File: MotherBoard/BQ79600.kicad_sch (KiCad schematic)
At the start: 10 parts, among them IC501 BQ79600PWRQ1

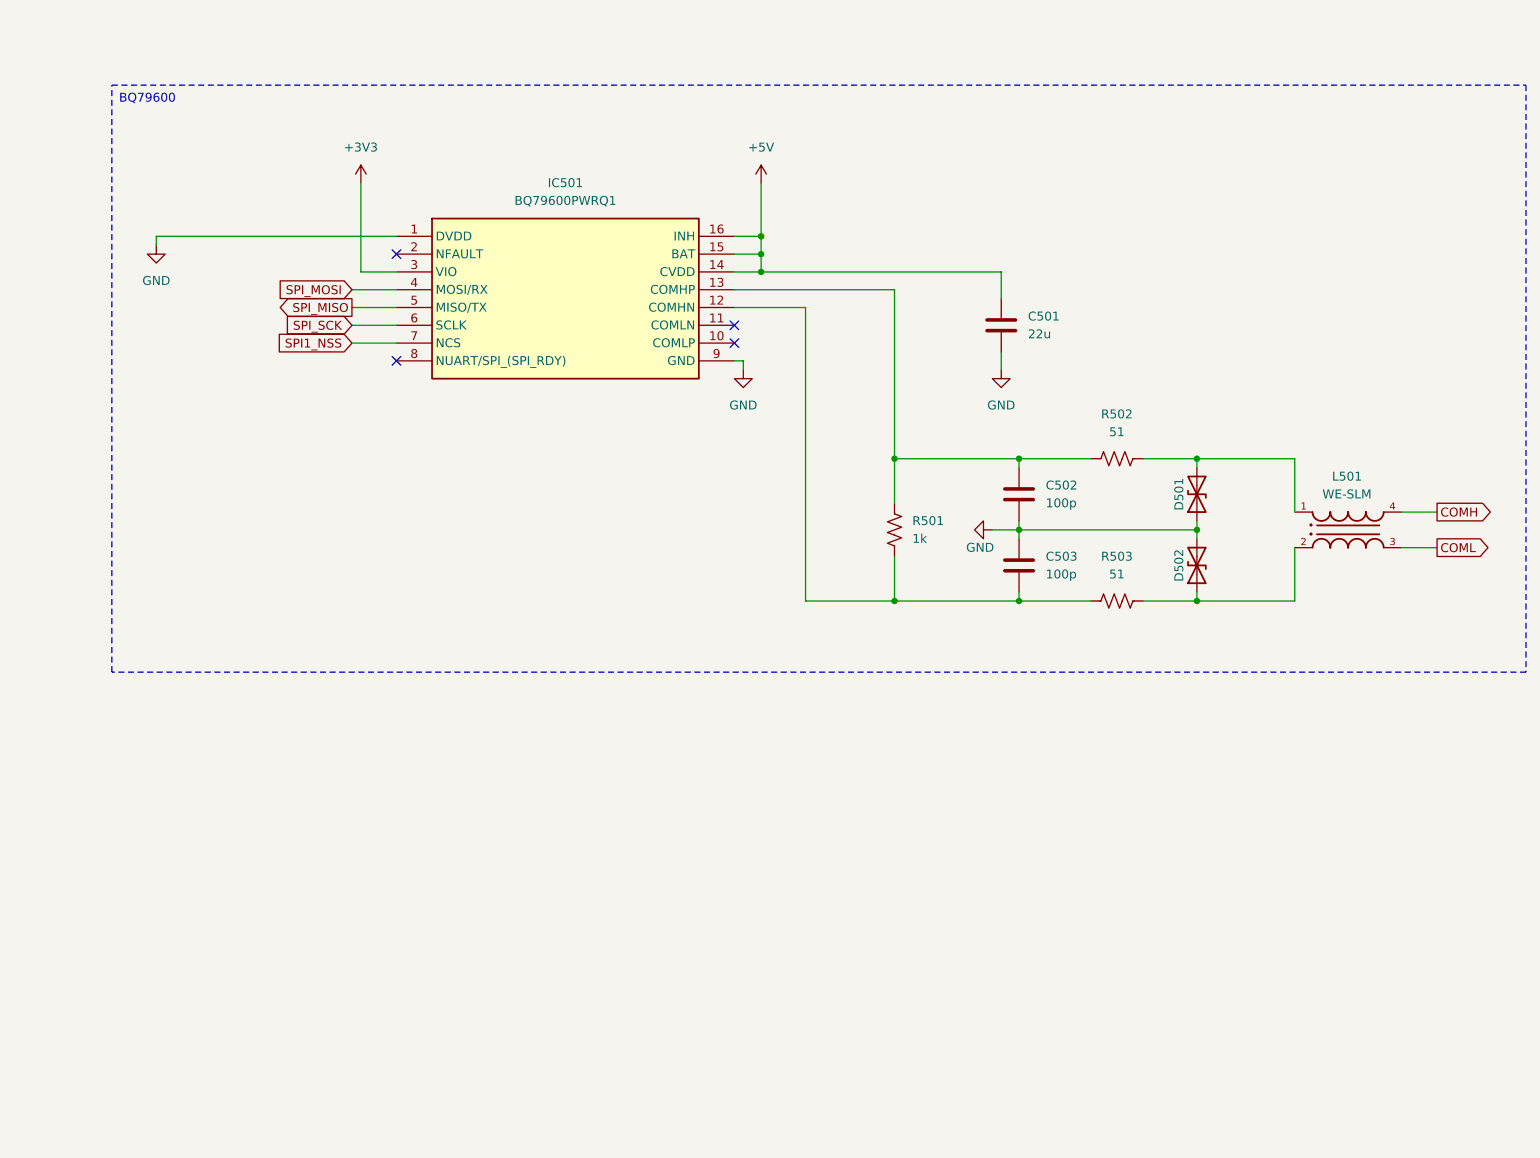
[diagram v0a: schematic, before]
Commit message: Fixed BQ79600 + minor changes
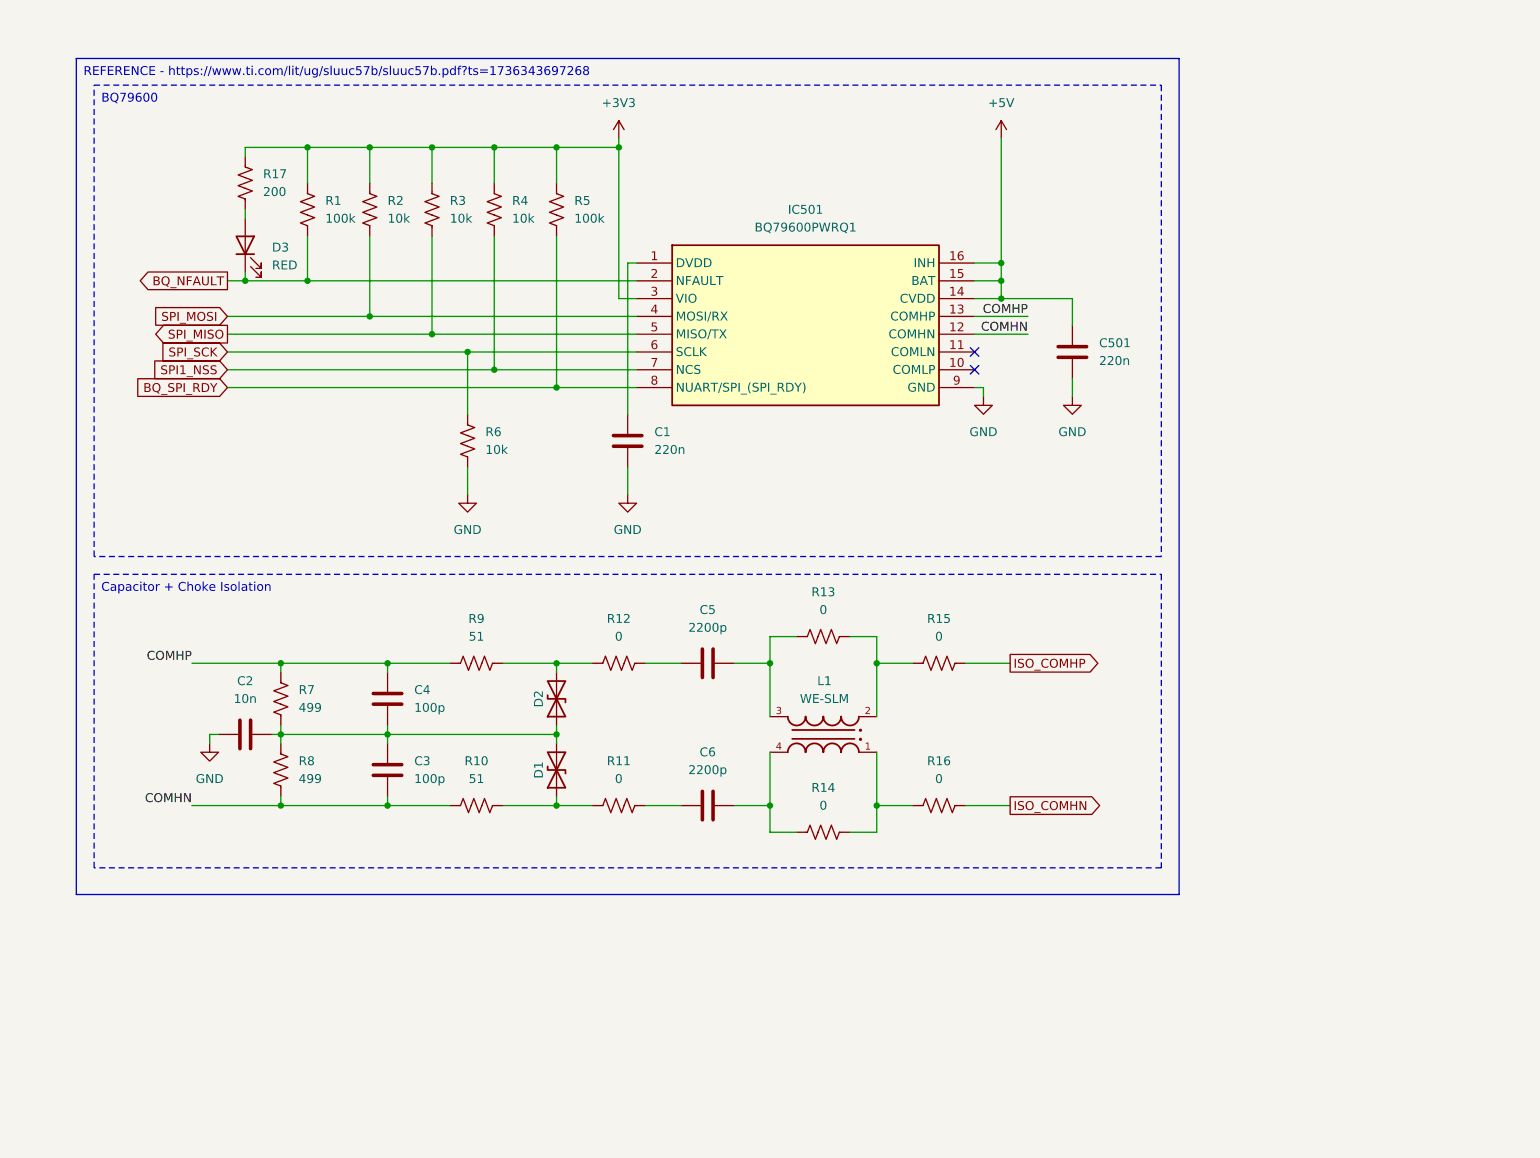
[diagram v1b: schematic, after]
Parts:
- removed C502, C503: 100p, symbol Device:C
- removed D501, D502: D_TVS, Diode_SMD:D_SOD-323, symbol Device:D_TVS
- removed L501: WE-SLM, Transformer_WURTH:Isolation_Transformer, symbol Isolation_Transformer:WE-SLM
- removed R501: 1k, symbol Device:R_US
- removed R502, R503: 51, symbol Device:R_US
- added C1: 220n, symbol Device:C
- added C2: 10n, symbol Device:C
- added C3, C4: 100p, symbol Device:C
- added C5, C6: 2200p, symbol Device:C
- added D1, D2: D_TVS, Diode_SMD:D_SOD-323, symbol Device:D_TVS
- added D3: RED, symbol Device:LED
- added L1: WE-SLM, WE-SLM:WE-SLM, symbol CommonModeChoke_Wurth:WE-SLM
- added R1, R5: 100k, symbol Device:R_US
- added R10, R9: 51, symbol Device:R_US
- added R11, R12, R13, R14, R15, R16: 0, symbol Device:R_US
- added R17: 200, symbol Device:R_US
- added R2, R3, R4, R6: 10k, symbol Device:R_US
- added R7, R8: 499, symbol Device:R_US
- C501: value 22u -> 220n
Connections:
- net +3V3: now also R1.1, R17.1, R2.1, R3.1, R4.1, R5.1
- net GND: now also C1.1, C2.1, R6.2; no longer IC501.1 (DVDD)
- net SPI1_NSS: now also R4.2
- net SPI_MISO: now also R3.2
- net SPI_MOSI: now also R2.2
- net SPI_SCK: now also R6.1
- net COMHN: now reaches IC501.12 (COMHN)
- net COMHN: now also C3.1, R10.1, R8.2
- net COMHP: now reaches IC501.13 (COMHP)
- net COMHP: now also C4.2, R7.1, R9.1
- net BQ_NFAULT: now reaches IC501.2 (NFAULT)
- net BQ_NFAULT: now also D3.1 (K), R1.2
- net BQ_SPI_RDY: now reaches IC501.8 (NUART/SPI_(SPI_RDY))
- net BQ_SPI_RDY: now also R5.2
- new net: C2.2, C3.2, C4.1, D1.2 (A2), D2.1 (A1), R7.2, R8.1
- new net: C1.2, IC501.1 (DVDD)
- new net: L1.1, R14.2, R16.1
- new net: L1.2, R13.2, R15.1
- new net: C5.1, L1.3, R13.1
- new net: C6.1, L1.4, R14.1
- new net: D2.2 (A2), R12.1, R9.2
- new net: C5.2, R12.2
- new net: D3.2 (A), R17.2
- new net: D1.1 (A1), R10.2, R11.1
- new net: C6.2, R11.2
- new net ISO_COMHN: R16.2
- new net ISO_COMHP: R15.2
- no-connect marks 4 -> 2
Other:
- company: (none) -> FSAE LSU
- moved on the sheet: C501, IC501

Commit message: Fixed CAN tranceivers + added relay driver circuit + fixed relative file paths for 3D models + finished PSU but still need correct 3D model
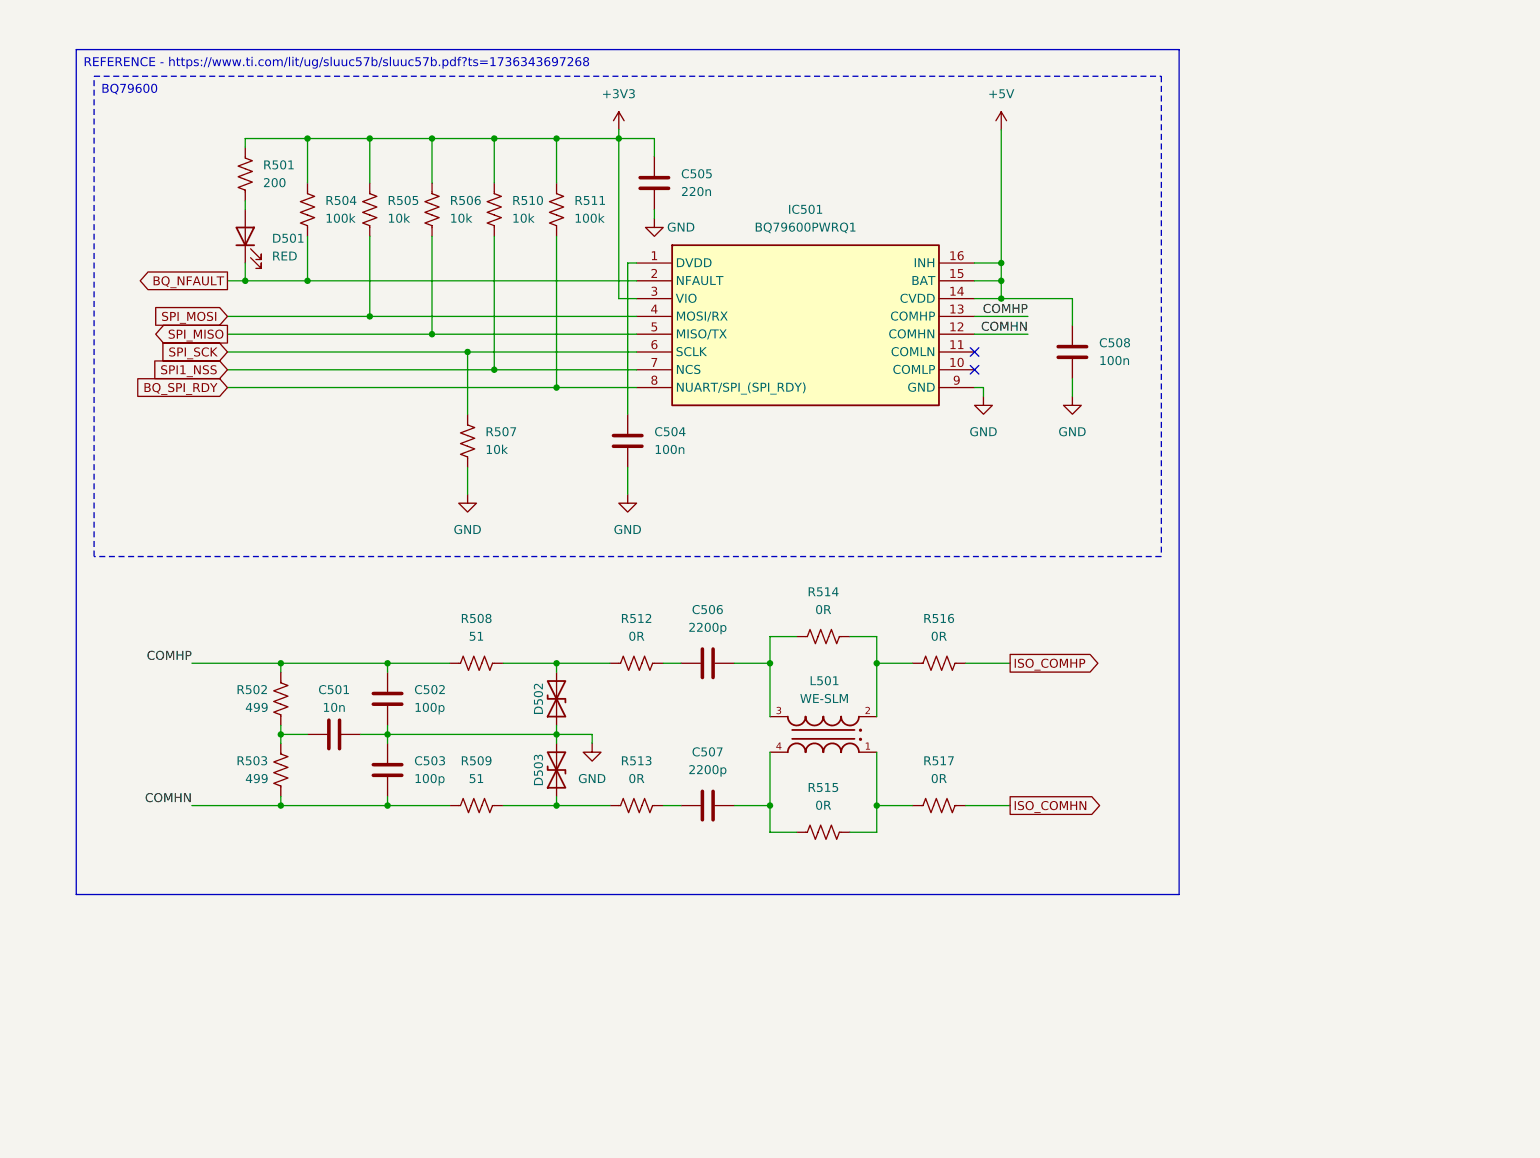
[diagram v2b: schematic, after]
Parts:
- added C505: 220n, symbol Device:C
- C504: renamed from C1; value 220n -> 100n
- C508: renamed from C501; value 220n -> 100n
- R512: renamed from R12; value 0 -> 0R
- R513: renamed from R11; value 0 -> 0R
- R514: renamed from R13; value 0 -> 0R
- R515: renamed from R14; value 0 -> 0R
- R516: renamed from R15; value 0 -> 0R
- R517: renamed from R16; value 0 -> 0R
- renumbered C2 to C501, C4 to C502, C3 to C503, C5 to C506, C6 to C507, D3 to D501, D2 to D502, D1 to D503, L1 to L501, R17 to R501, R7 to R502, R8 to R503, R1 to R504, R2 to R505, R3 to R506, R6 to R507, R9 to R508, R10 to R509, R4 to R510, R5 to R511
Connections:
- net +3V3: now also C505.1
- net GND: now also C502.1, C503.2, D502.1 (A1), D503.2 (A2), C505.2
- new net: C501.2, R502.2, R503.1
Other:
- moved on the sheet: C501, D501, R501, R512, R513

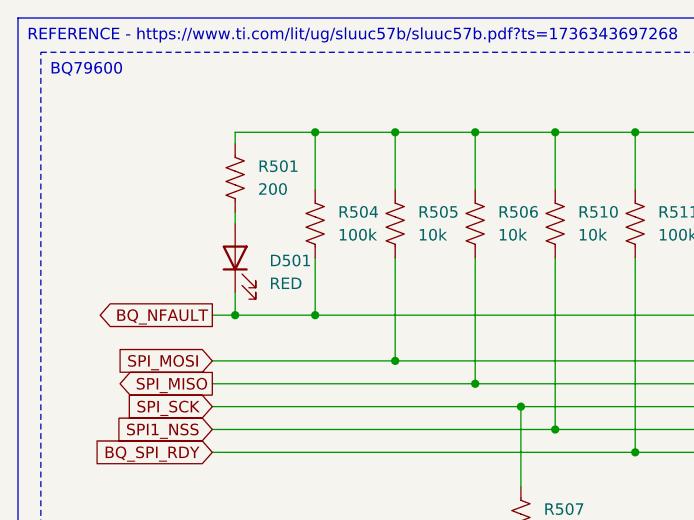
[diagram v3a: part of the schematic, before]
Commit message: Fixed 3D model paths. Finished PSU ORing shcematic.
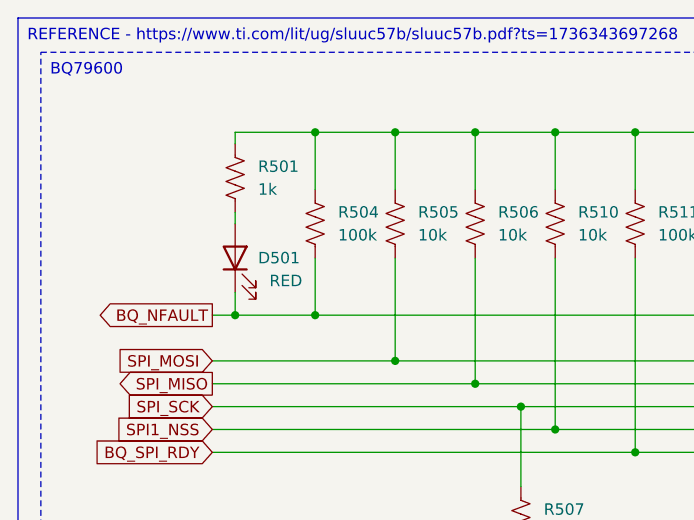
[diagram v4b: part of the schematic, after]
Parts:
- R501: value 200 -> 1k
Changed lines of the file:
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@@
 			)
 		)
-		(property "Value" "200"
+		(property "Value" "1k"
 			(at 52.07 40.64 0)
 			(effects
@@
 		(on_board yes)
 		(dnp no)
-		(fields_autoplaced yes)
 		(property "Reference" "D501"
-			(at 53.34 48.5774 90)
+			(at 52.07 48.26 90)
 			(effects
 				(font
@@
 		)
 		(property "Value" "RED"
-			(at 53.34 51.1174 90)
-			(effects
-				(font
+			(at 53.34 50.8 90)
+			(effects
+				(font

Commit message: Added more 3D models
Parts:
- C501, C504, C508: footprint (none) -> Capacitor_SMD:C_0402_1005Metric
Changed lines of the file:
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@@
 			)
 		)
-		(property "Footprint" ""
+		(property "Footprint" "Capacitor_SMD:C_0402_1005Metric"
 			(at 58.42 120.3452 0)
 			(effects
@@
 			)
 		)
-		(property "Footprint" ""
+		(property "Footprint" "Capacitor_SMD:C_0402_1005Metric"
 			(at 103.1748 73.66 0)
 			(effects
@@
 			)
 		)
-		(property "Footprint" ""
+		(property "Footprint" "Capacitor_SMD:C_0402_1005Metric"
 			(at 168.6052 68.58 0)
 			(effects

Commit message: Fixed relative paths + 90% footprints done + organized PCB for layout + found JLC part #s for manufacturing
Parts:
- C502, C503, C505, C506, C507: footprint (none) -> Capacitor_SMD:C_0402_1005Metric
- D501: footprint (none) -> LED_SMD:LED_0603_1608Metric
- L501: Manufacturer_Part_Number (none) -> 744242471
- R501, R504, R505, R506, R507, R510, R511, R512, R513, R514, R515, R516, R517: footprint (none) -> Resistor_SMD:R_0402_1005Metric

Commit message: Completed BOM except inductors
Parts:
- C501: Manufacturer_Part_Number (none) -> CC0402KRX7R9BB103
- C502, C503: Manufacturer_Part_Number (none) -> 0402CG101J500NT
- C504, C508: value 100n -> 220n; footprint Capacitor_SMD:C_0402_1005Metric -> Capacitor_SMD:C_0603_1608Metric; Manufacturer_Part_Number (none) -> CL10B224KA8NNNC
- C505: footprint Capacitor_SMD:C_0402_1005Metric -> Capacitor_SMD:C_0603_1608Metric; Manufacturer_Part_Number (none) -> CL10B224KA8NNNC
- C506, C507: footprint Capacitor_SMD:C_0402_1005Metric -> Capacitor_SMD:C_0805_2012Metric; Manufacturer_Part_Number (none) -> CL21C222JBFNNNE
- D501: Manufacturer_Part_Number (none) -> KT-0603R
- R501, R505, R506, R507, R510: Manufacturer_Part_Number (none) -> 0402WGF1001TCE
- R502, R503: footprint (none) -> Resistor_SMD:R_0603_1608Metric; Manufacturer_Part_Number (none) -> 0603WAF4990T5E
- R504, R511: Manufacturer_Part_Number (none) -> 0402WGF1003TCE
- R508, R509: footprint (none) -> Resistor_SMD:R_1206_3216Metric; Manufacturer_Part_Number (none) -> C18019
- R512, R513, R514, R515, R516, R517: footprint Resistor_SMD:R_0402_1005Metric -> Resistor_SMD:R_0805_2012Metric; Manufacturer_Part_Number (none) -> 0805W8F0000T5E

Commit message: Finished layout need to route
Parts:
- added C502: 10n, Capacitor_SMD:C_0402_1005Metric, symbol Device:C
- added C505, C506: 100p, Capacitor_SMD:C_0402_1005Metric, symbol Device:C
- added C511, C512: 2200p, Capacitor_SMD:C_0805_2012Metric, symbol Device:C
- added D504, D505: D_TVS, Diode_SMD:D_SOD-323, symbol Device:D_TVS
- added L502: WE-SLM, WE-SLM:WE-SLM, symbol CommonModeChoke_Wurth:WE-SLM
- added R504, R505: 499, Resistor_SMD:R_0603_1608Metric, symbol Device:R_US
- added R512, R513: 51, Resistor_SMD:R_1206_3216Metric, symbol Device:R_US
- added R518, R519, R522, R523, R526, R527: 0R, Resistor_SMD:R_0805_2012Metric, symbol Device:R_US
- renumbered C502 to C503, C503 to C504, C504 to C507, C505 to C508, C506 to C509, C507 to C510, C508 to C513, R504 to R506, R505 to R507, R506 to R508, R507 to R509, R508 to R510, R509 to R511, R510 to R514, R511 to R515, R512 to R516, R513 to R517, R514 to R520, R515 to R521, R516 to R524, R517 to R525
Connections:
- net GND: now also C502.1, C505.1, C506.2, D504.1 (A1), D505.2 (A2)
- net COMLP: now reaches IC501.10 (COMLP)
- net COMLP: now also C505.2, R504.1, R512.1
- net COMLN: now reaches IC501.11 (COMLN)
- net COMLN: now also C506.1, R505.2, R513.1
- new net: C511.1, L502.3, R522.1
- new net: L502.2, R522.2, R526.1
- new net: D504.2 (A2), R512.2, R518.1
- new net: C511.2, R518.2
- new net: D505.1 (A1), R513.2, R519.1
- new net: C502.2, R504.2, R505.1
- new net: C512.1, L502.4, R523.1
- new net: C512.2, R519.2
- new net: L502.1, R523.2, R527.1
- new net ISO_COMLN: R527.2
- new net ISO_COMLP: R526.2
- no-connect marks 2 -> 0
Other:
- moved on the sheet: C501, C503, C504, C507, C508, C509, C510, C513, D501, D502, D503, IC501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
